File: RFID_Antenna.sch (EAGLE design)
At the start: 16 parts, among them J1 U.FL

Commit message: Caopy Murata Design w/ Transparency for x02
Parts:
- C1, C2, C3, C4, C5, C6: device special_parts:CAPACITOR0402 -> special_parts:CAPACITORM0402
- FRAME1: DESIGNER (none) -> Owen Lyke; REV (none) -> x02
- L1: device special_parts:INDUCTOR0402 -> special_parts:INDUCTORM0402
- L2, L3, L4, L5: device special_parts:INDUCTOR0603 -> special_parts:INDUCTORM0603
- R1: device special_parts:RESISTOR0402 -> special_parts:RESISTORM0402
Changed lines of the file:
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@@
 </classes>
 <parts>
-<part name="FRAME1" library="SparkFun-Aesthetics" deviceset="FRAME-LETTER" device=""/>
-<part name="R1" library="special_parts" deviceset="RESISTOR" device="0402" value="4.28k"/>
-<part name="C1" library="special_parts" deviceset="CAPACITOR" device="0402" value="9.3 pF"/>
-<part name="C2" library="special_parts" deviceset="CAPACITOR" device="0402" value="9.3 pF"/>
-<part name="C3" library="special_parts" deviceset="CAPACITOR" device="0402" value="9.0 pF"/>
-<part name="C4" library="special_parts" deviceset="CAPACITOR" device="0402" value="9.0 pF"/>
-<part name="L1" library="special_parts" deviceset="INDUCTOR" device="0402" value="0.26 uH"/>
-<part name="L2" library="special_parts" deviceset="INDUCTOR" device="0603" value="0.26 uH"/>
-<part name="L3" library="special_parts" deviceset="INDUCTOR" device="0603" value="0.26 uH"/>
-<part name="L4" library="special_parts" deviceset="INDUCTOR" device="0603" value="0.24 uH"/>
-<part name="L5" library="special_parts" deviceset="INDUCTOR" device="0603" value="0.24 uH"/>
-<part name="C5" library="special_parts" deviceset="CAPACITOR" device="0402" value="5.66 pF"/>
-<part name="C6" library="special_parts" deviceset="CAPACITOR" device="0402" value="5.66 pF"/>
+<part name="FRAME1" library="SparkFun-Aesthetics" deviceset="FRAME-LETTER" device="">
+<attribute name="DESIGNER" value="Owen Lyke"/>
+<attribute name="REV" value="x02"/>
+</part>
+<part name="R1" library="special_parts" deviceset="RESISTOR" device="M0402" value="4.28k"/>
+<part name="C1" library="special_parts" deviceset="CAPACITOR" device="M0402" value="9.3 pF"/>
+<part name="C2" library="special_parts" deviceset="CAPACITOR" device="M0402" value="9.3 pF"/>
+<part name="C3" library="special_parts" deviceset="CAPACITOR" device="M0402" value="9.0 pF"/>
+<part name="C4" library="special_parts" deviceset="CAPACITOR" device="M0402" value="9.0 pF"/>
+<part name="L1" library="special_parts" deviceset="INDUCTOR" device="M0402" value="0.26 uH"/>
+<part name="L2" library="special_parts" deviceset="INDUCTOR" device="M0603" value="0.26 uH"/>
+<part name="L3" library="special_parts" deviceset="INDUCTOR" device="M0603" value="0.26 uH"/>
+<part name="L4" library="special_parts" deviceset="INDUCTOR" device="M0603" value="0.24 uH"/>
+<part name="L5" library="special_parts" deviceset="INDUCTOR" device="M0603" value="0.24 uH"/>
+<part name="C5" library="special_parts" deviceset="CAPACITOR" device="M0402" value="5.66 pF"/>
+<part name="C6" library="special_parts" deviceset="CAPACITOR" device="M0402" value="5.66 pF"/>
 <part name="GND1" library="SparkFun-PowerSymbols" deviceset="GND" device=""/>
 <part name="J1" library="SparkFun-Connectors" deviceset="U.FL" device="" value="U.FL"/>

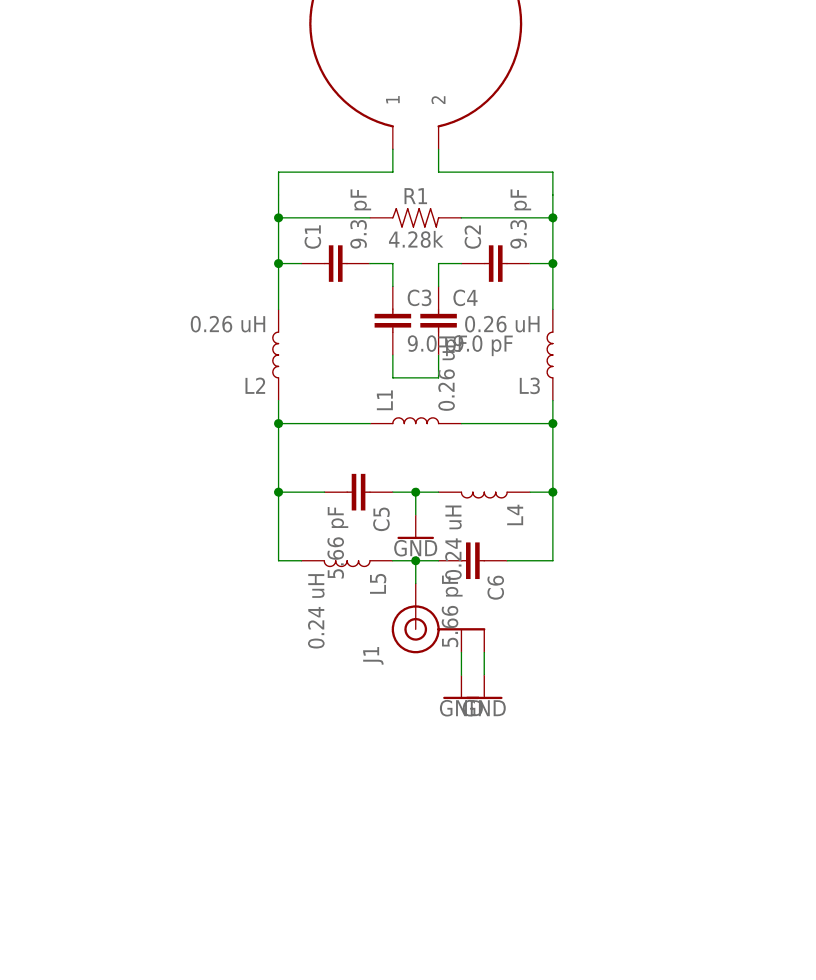
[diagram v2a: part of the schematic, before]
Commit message: Prettified schematic (and fixed component values)
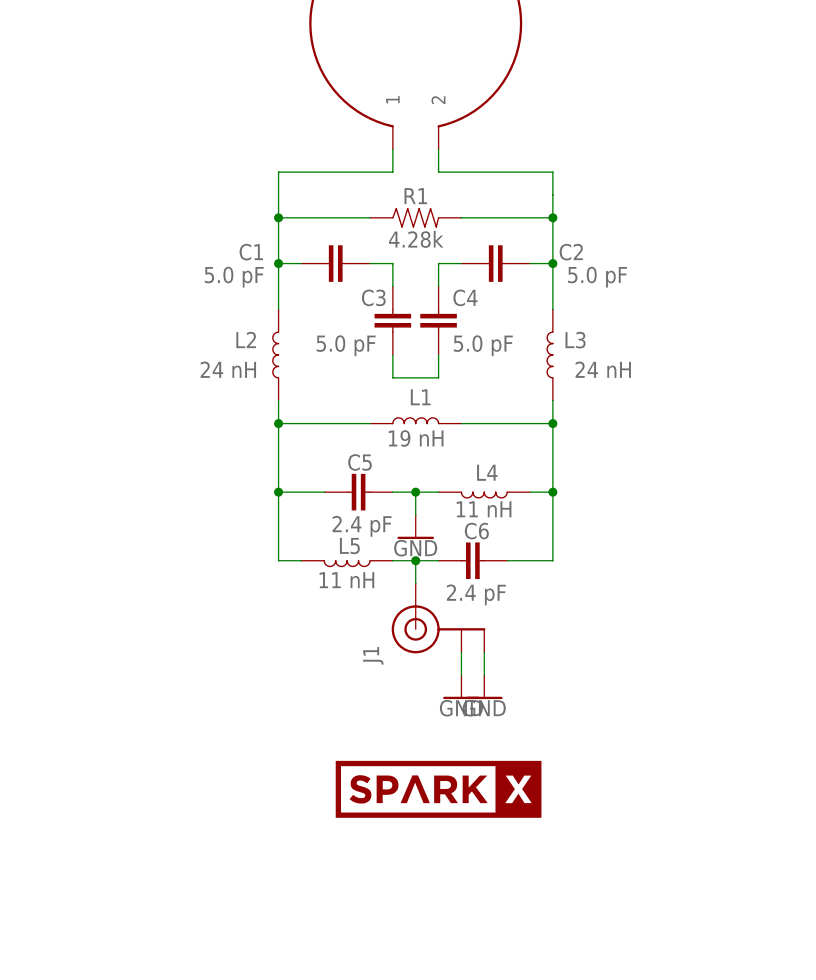
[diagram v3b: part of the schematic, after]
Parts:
- added U$12: SPARKX-LOGO6, SparkX:SPARKX-LOGO6
- C1, C2: value 9.3 pF -> 5.0 pF
- C3, C4: value 9.0 pF -> 5.0 pF
- C5, C6: value 5.66 pF -> 2.4 pF
- L1: value 0.26 uH -> 19 nH
- L2, L3: value 0.26 uH -> 24 nH
- L4, L5: value 0.24 uH -> 11 nH
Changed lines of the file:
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@@
 </part>
 <part name="R1" library="special_parts" deviceset="RESISTOR" device="M0402" value="4.28k"/>
-<part name="C1" library="special_parts" deviceset="CAPACITOR" device="M0402" value="9.3 pF"/>
-<part name="C2" library="special_parts" deviceset="CAPACITOR" device="M0402" value="9.3 pF"/>
-<part name="C3" library="special_parts" deviceset="CAPACITOR" device="M0402" value="9.0 pF"/>
-<part name="C4" library="special_parts" deviceset="CAPACITOR" device="M0402" value="9.0 pF"/>
-<part name="L1" library="special_parts" deviceset="INDUCTOR" device="M0402" value="0.26 uH"/>
-<part name="L2" library="special_parts" deviceset="INDUCTOR" device="M0603" value="0.26 uH"/>
-<part name="L3" library="special_parts" deviceset="INDUCTOR" device="M0603" value="0.26 uH"/>
-<part name="L4" library="special_parts" deviceset="INDUCTOR" device="M0603" value="0.24 uH"/>
-<part name="L5" library="special_parts" deviceset="INDUCTOR" device="M0603" value="0.24 uH"/>
-<part name="C5" library="special_parts" deviceset="CAPACITOR" device="M0402" value="5.66 pF"/>
-<part name="C6" library="special_parts" deviceset="CAPACITOR" device="M0402" value="5.66 pF"/>
+<part name="C1" library="special_parts" deviceset="CAPACITOR" device="M0402" value="5.0 pF"/>
+<part name="C2" library="special_parts" deviceset="CAPACITOR" device="M0402" value="5.0 pF"/>
+<part name="C3" library="special_parts" deviceset="CAPACITOR" device="M0402" value="5.0 pF"/>
+<part name="C4" library="special_parts" deviceset="CAPACITOR" device="M0402" value="5.0 pF"/>
+<part name="L1" library="special_parts" deviceset="INDUCTOR" device="M0402" value="19 nH"/>
+<part name="L2" library="special_parts" deviceset="INDUCTOR" device="M0603" value="24 nH"/>
+<part name="L3" library="special_parts" deviceset="INDUCTOR" device="M0603" value="24 nH"/>
+<part name="L4" library="special_parts" deviceset="INDUCTOR" device="M0603" value="11 nH"/>
+<part name="L5" library="special_parts" deviceset="INDUCTOR" device="M0603" value="11 nH"/>
+<part name="C5" library="special_parts" deviceset="CAPACITOR" device="M0402" value="2.4 pF"/>
+<part name="C6" library="special_parts" deviceset="CAPACITOR" device="M0402" value="2.4 pF"/>
 <part name="GND1" library="SparkFun-PowerSymbols" deviceset="GND" device=""/>
 <part name="J1" library="SparkFun-Connectors" deviceset="U.FL" device="" value="U.FL"/>
@@
 <part name="U$1" library="special_parts" deviceset="ANTENNA" device=""/>
 <part name="U$2" library="SparkFun-Aesthetics" deviceset="SPECIAL_INSTRUCTIONS" device="-ORDERING"/>
+<part name="U$12" library="SparkX" deviceset="SPARKX-LOGO" device="6"/>
 </parts>
 <sheets>
@@
 <instance part="FRAME1" gate="G$1" x="0" y="0"/>
 <instance part="FRAME1" gate="V" x="147.32" y="0"/>
-<instance part="R1" gate="G$1" x="114.3" y="127"/>
-<instance part="C1" gate="G$1" x="106.68" y="121.92" rot="R90"/>
-<instance part="C2" gate="G$1" x="124.46" y="121.92" rot="R90"/>
-<instance part="C3" gate="G$1" x="111.76" y="114.3"/>
-<instance part="C4" gate="G$1" x="116.84" y="114.3"/>
-<instance part="L1" gate="G$1" x="114.3" y="104.14" rot="R90"/>
-<instance part="L2" gate="G$1" x="99.06" y="111.76" rot="R180"/>
-<instance part="L3" gate="G$1" x="129.54" y="111.76" rot="R180"/>
-<instance part="L4" gate="G$1" x="121.92" y="96.52" rot="R270"/>
-<instance part="L5" gate="G$1" x="106.68" y="88.9" rot="R270"/>
-<instance part="C5" gate="G$1" x="106.68" y="96.52" rot="R270"/>
-<instance part="C6" gate="G$1" x="119.38" y="88.9" rot="R270"/>
-<instance part="GND1" gate="1" x="114.3" y="91.44"/>
+<instance part="R1" gate="G$1" x="114.3" y="127" smashed="yes">
+<attribute name="NAME" x="114.3" y="128.524" size="1.778" layer="95" font="vector" align="bottom-center"/>
+<attribute name="VALUE" x="114.3" y="125.476" size="1.778" layer="96" font="vector" align="top-center"/>
+</instance>
+<instance part="C1" gate="G$1" x="106.68" y="121.92" smashed="yes" rot="R90">
+<attribute name="NAME" x="97.536" y="124.079" size="1.778" layer="95" font="vector" rot="R180"/>
+<attribute name="VALUE" x="97.536" y="121.539" size="1.778" layer="96" font="vector" rot="R180"/>
+</instance>
+<instance part="C2" gate="G$1" x="124.46" y="121.92" smashed="yes" rot="R90">
+<attribute name="NAME" x="133.096" y="124.079" size="1.778" layer="95" font="vector" rot="R180"/>
+<attribute name="VALUE" x="131.064" y="119.761" size="1.778" layer="96" font="vector"/>
+</instance>
+<instance part="C3" gate="G$1" x="111.76" y="114.3" smashed="yes">
+<attribute name="NAME" x="108.204" y="117.221" size="1.778" layer="95" font="vector"/>
+<attribute name="VALUE" x="103.124" y="112.141" size="1.778" layer="96" font="vector"/>
+</instance>
+<instance part="C4" gate="G$1" x="116.84" y="114.3" smashed="yes">
+<attribute name="NAME" x="118.364" y="117.221" size="1.778" layer="95" font="vector"/>
+<attribute name="VALUE" x="118.364" y="112.141" size="1.778" layer="96" font="vector"/>
+</instance>
+<instance part="L1" gate="G$1" x="114.3" y="104.14" smashed="yes" rot="R90">
+<attribute name="NAME" x="113.538" y="106.172" size="1.778" layer="95" font="vector"/>
+<attribute name="VALUE" x="117.602" y="101.6" size="1.778" layer="96" font="vector" rot="R180" align="top-left"/>
+</instance>
+<instance part="L2" gate="G$1" x="99.06" y="111.76" smashed="yes" rot="R180">
+<attribute name="NAME" x="96.774" y="114.3" size="1.778" layer="95" font="vector" rot="R180"/>
+<attribute name="VALUE" x="96.774" y="109.22" size="1.778" layer="96" font="vector" rot="R180" align="top-left"/>
+</instance>
+<instance part="L3" gate="G$1" x="129.54" y="111.76" smashed="yes" rot="R180">
+<attribute name="NAME" x="133.35" y="114.3" size="1.778" layer="95" font="vector" rot="R180"/>
+<attribute name="VALUE" x="138.43" y="109.22" size="1.778" layer="96" font="vector" rot="R180" align="top-left"/>
+</instance>
+<instance part="L4" gate="G$1" x="121.92" y="96.52" smashed="yes" rot="R270">
+<attribute name="NAME" x="120.904" y="97.79" size="1.778" layer="95" font="vector"/>
+<attribute name="VALUE" x="118.618" y="95.504" size="1.778" layer="96" font="vector" align="top-left"/>
+</instance>
+<instance part="L5" gate="G$1" x="106.68" y="88.9" smashed="yes" rot="R270">
+<attribute name="NAME" x="105.664" y="89.662" size="1.778" layer="95" font="vector"/>
+<attribute name="VALUE" x="103.378" y="87.63" size="1.778" layer="96" font="vector" align="top-left"/>
+</instance>
+<instance part="C5" gate="G$1" x="106.68" y="96.52" smashed="yes" rot="R270">
+<attribute name="NAME" x="106.68" y="98.933" size="1.778" layer="95" font="vector"/>
+<attribute name="VALUE" x="104.902" y="92.075" size="1.778" layer="96" font="vector"/>
+</instance>
+<instance part="C6" gate="G$1" x="119.38" y="88.9" smashed="yes" rot="R270">
+<attribute name="NAME" x="119.634" y="91.313" size="1.778" layer="95" font="vector"/>
+<attribute name="VALUE" x="117.602" y="84.455" size="1.778" layer="96" font="vector"/>
+</instance>
+<instance part="GND1" gate="1" x="114.3" y="91.44" smashed="yes">
+<attribute name="VALUE" x="114.3" y="91.186" size="1.778" layer="96" align="top-center"/>
+</instance>
 <instance part="J1" gate="G$1" x="114.3" y="81.28" rot="R90"/>
 <instance part="GND2" gate="1" x="119.38" y="73.66"/>
@@
 <instance part="U$1" gate="G$1" x="114.3" y="137.16"/>
 <instance part="U$2" gate="G$1" x="223.52" y="38.1"/>
+<instance part="U$12" gate="G$1" x="116.84" y="63.5"/>
 </instances>
 <busses>

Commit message: Updated parts with PROD_ID and Eagle Library for production
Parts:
- C1, C2, C3, C4: device special_parts:CAPACITORM0402 -> SparkFun-Capacitors:5.0PF-0402
- C5, C6: device special_parts:CAPACITORM0402 -> SparkFun-Capacitors:2.4PF-0402
- L1: device special_parts:INDUCTORM0402 -> SparkFun-Coils:19NH-0402
- L2, L3: device special_parts:INDUCTORM0603 -> SparkFun-Coils:24NH-0603
- L4, L5: device special_parts:INDUCTORM0603 -> SparkFun-Coils:11NH-0603
- R1: value 4.28k -> 4.3k; device special_parts:RESISTORM0402 -> SparkFun-Resistors:4.3KOHM-0402
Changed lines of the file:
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@@
 <?xml version="1.0" encoding="utf-8"?>
 <!DOCTYPE eagle SYSTEM "eagle.dtd">
-<eagle version="9.1.3">
+<eagle version="9.3.0">
 <drawing>
 <settings>
@@
 <layer number="1" name="Top" color="4" fill="1" visible="no" active="no"/>
 <layer number="2" name="Route2" color="1" fill="3" visible="no" active="no"/>
+<layer number="3" name="Route3" color="4" fill="3" visible="no" active="no"/>
+<layer number="4" name="Route4" color="1" fill="4" visible="no" active="no"/>
+<layer number="5" name="Route5" color="4" fill="4" visible="no" active="no"/>
+<layer number="6" name="Route6" color="1" fill="8" visible="no" active="no"/>
+<layer number="7" name="Route7" color="4" fill="8" visible="no" active="no"/>
+<layer number="8" name="Route8" color="1" fill="2" visible="no" active="no"/>
+<layer number="9" name="Route9" color="4" fill="2" visible="no" active="no"/>
+<layer number="10" name="Route10" color="1" fill="7" visible="no" active="no"/>
+<layer number="11" name="Route11" color="4" fill="7" visible="no" active="no"/>
+<layer number="12" name="Route12" color="1" fill="5" visible="no" active="no"/>
+<layer number="13" name="Route13" color="4" fill="5" visible="no" active="no"/>
+<layer number="14" name="Route14" color="1" fill="6" visible="no" active="no"/>
 <layer number="15" name="Route15" color="4" fill="6" visible="no" active="no"/>
 <layer number="16" name="Bottom" color="1" fill="1" visible="no" active="no"/>
@@
 <attribute name="REV" value="x02"/>
 </part>
-<part name="R1" library="special_parts" deviceset="RESISTOR" device="M0402" value="4.28k"/>
-<part name="C1" library="special_parts" deviceset="CAPACITOR" device="M0402" value="5.0 pF"/>
-<part name="C2" library="special_parts" deviceset="CAPACITOR" device="M0402" value="5.0 pF"/>
-<part name="C3" library="special_parts" deviceset="CAPACITOR" device="M0402" value="5.0 pF"/>
-<part name="C4" library="special_parts" deviceset="CAPACITOR" device="M0402" value="5.0 pF"/>
-<part name="L1" library="special_parts" deviceset="INDUCTOR" device="M0402" value="19 nH"/>
-<part name="L2" library="special_parts" deviceset="INDUCTOR" device="M0603" value="24 nH"/>
-<part name="L3" library="special_parts" deviceset="INDUCTOR" device="M0603" value="24 nH"/>
-<part name="L4" library="special_parts" deviceset="INDUCTOR" device="M0603" value="11 nH"/>
-<part name="L5" library="special_parts" deviceset="INDUCTOR" device="M0603" value="11 nH"/>
-<part name="C5" library="special_parts" deviceset="CAPACITOR" device="M0402" value="2.4 pF"/>
-<part name="C6" library="special_parts" deviceset="CAPACITOR" device="M0402" value="2.4 pF"/>
+<part name="R1" library="SparkFun-Resistors" deviceset="4.3KOHM" device="-0402" value="4.3k"/>
+<part name="C1" library="SparkFun-Capacitors" deviceset="5.0PF" device="-0402" value="5.0 pF"/>
+<part name="C2" library="SparkFun-Capacitors" deviceset="5.0PF" device="-0402" value="5.0 pF"/>
+<part name="C3" library="SparkFun-Capacitors" deviceset="5.0PF" device="-0402" value="5.0 pF"/>
+<part name="C4" library="SparkFun-Capacitors" deviceset="5.0PF" device="-0402" value="5.0 pF"/>
+<part name="L1" library="SparkFun-Coils" deviceset="19NH" device="-0402" value="19 nH"/>
+<part name="L2" library="SparkFun-Coils" deviceset="24NH" device="-0603" value="24 nH"/>
+<part name="L3" library="SparkFun-Coils" deviceset="24NH" device="-0603" value="24 nH"/>
+<part name="L4" library="SparkFun-Coils" deviceset="11NH" device="-0603" value="11 nH"/>
+<part name="L5" library="SparkFun-Coils" deviceset="11NH" device="-0603" value="11 nH"/>
+<part name="C5" library="SparkFun-Capacitors" deviceset="2.4PF" device="-0402" value="2.4 pF"/>
+<part name="C6" library="SparkFun-Capacitors" deviceset="2.4PF" device="-0402" value="2.4 pF"/>
 <part name="GND1" library="SparkFun-PowerSymbols" deviceset="GND" device=""/>
 <part name="J1" library="SparkFun-Connectors" deviceset="U.FL" device="" value="U.FL"/>
@@
 </plain>
 <instances>
-<instance part="FRAME1" gate="G$1" x="0" y="0"/>
-<instance part="FRAME1" gate="V" x="147.32" y="0"/>
+<instance part="FRAME1" gate="G$1" x="0" y="0" smashed="yes"/>
+<instance part="FRAME1" gate="V" x="147.32" y="0" smashed="yes">
+<attribute name="LAST_DATE_TIME" x="160.02" y="1.27" size="2.54" layer="94" font="vector"/>
+<attribute name="SHEET" x="233.68" y="1.27" size="2.54" layer="94" font="vector"/>
+<attribute name="DRAWING_NAME" x="162.814" y="17.78" size="2.7432" layer="94" font="vector"/>
+<attribute name="DESIGNER" x="170.434" y="11.176" size="2.7432" layer="94" font="vector"/>
+<attribute name="REV" x="236.22" y="6.604" size="2.7432" layer="94" font="vector"/>
+</instance>
 <instance part="R1" gate="G$1" x="114.3" y="127" smashed="yes">
 <attribute name="NAME" x="114.3" y="128.524" size="1.778" layer="95" font="vector" align="bottom-center"/>
@@
 <attribute name="VALUE" x="114.3" y="91.186" size="1.778" layer="96" align="top-center"/>
 </instance>
-<instance part="J1" gate="G$1" x="114.3" y="81.28" rot="R90"/>
-<instance part="GND2" gate="1" x="119.38" y="73.66"/>
-<instance part="GND3" gate="1" x="121.92" y="73.66"/>
-<instance part="U$1" gate="G$1" x="114.3" y="137.16"/>
-<instance part="U$2" gate="G$1" x="223.52" y="38.1"/>
-<instance part="U$12" gate="G$1" x="116.84" y="63.5"/>
+<instance part="J1" gate="G$1" x="114.3" y="81.28" smashed="yes" rot="R90">
+<attribute name="NAME" x="110.236" y="77.47" size="1.778" layer="95" rot="R90"/>
+</instance>
+<instance part="GND2" gate="1" x="119.38" y="73.66" smashed="yes">
+<attribute name="VALUE" x="119.38" y="73.406" size="1.778" layer="96" align="top-center"/>
+</instance>
+<instance part="GND3" gate="1" x="121.92" y="73.66" smashed="yes">
+<attribute name="VALUE" x="121.92" y="73.406" size="1.778" layer="96" align="top-center"/>
+</instance>
+<instance part="U$1" gate="G$1" x="114.3" y="137.16" smashed="yes"/>
+<instance part="U$2" gate="G$1" x="223.52" y="38.1" smashed="yes"/>
+<instance part="U$12" gate="G$1" x="116.84" y="63.5" smashed="yes"/>
 </instances>
 <busses>
